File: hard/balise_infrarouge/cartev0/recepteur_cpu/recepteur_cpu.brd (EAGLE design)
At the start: 55.6 x 47 mm, 14 parts, among them U1 ARDUINO_SHIELDNO_SILK

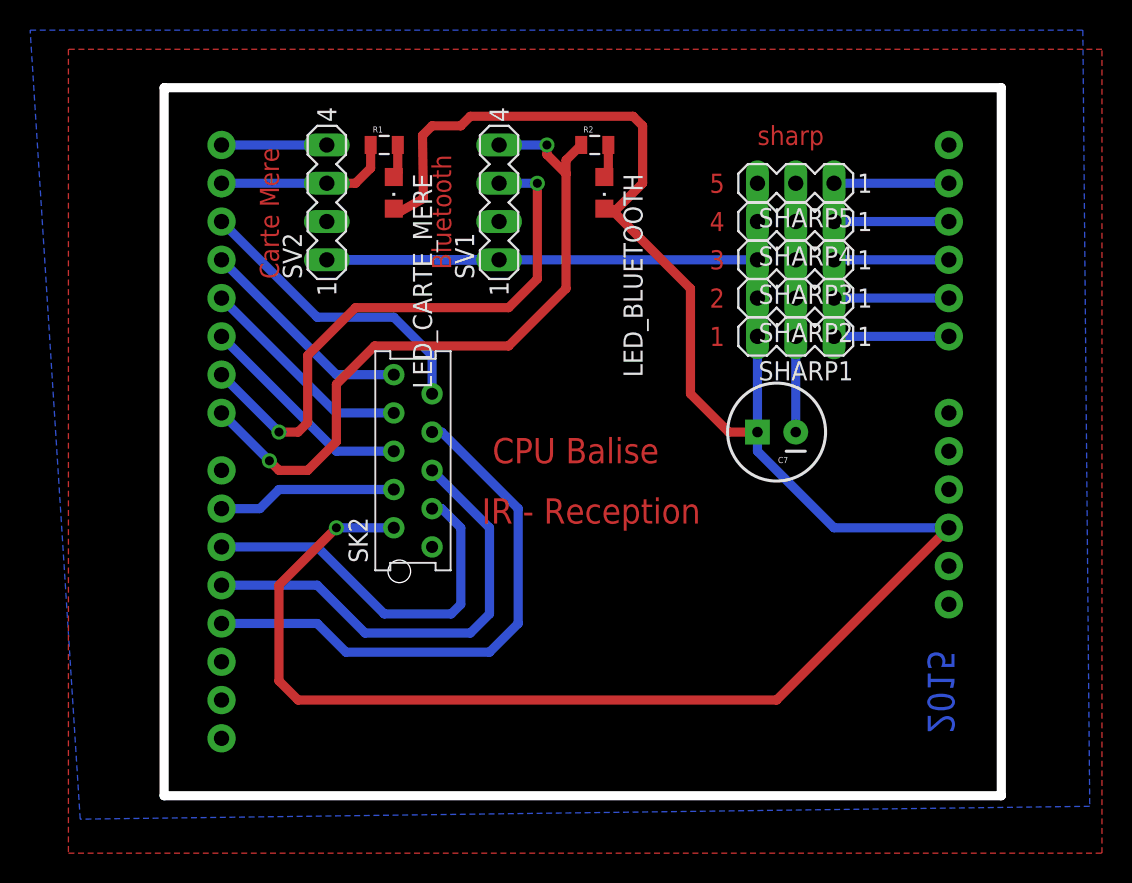
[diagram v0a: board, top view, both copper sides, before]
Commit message: maj carte extension nucleo
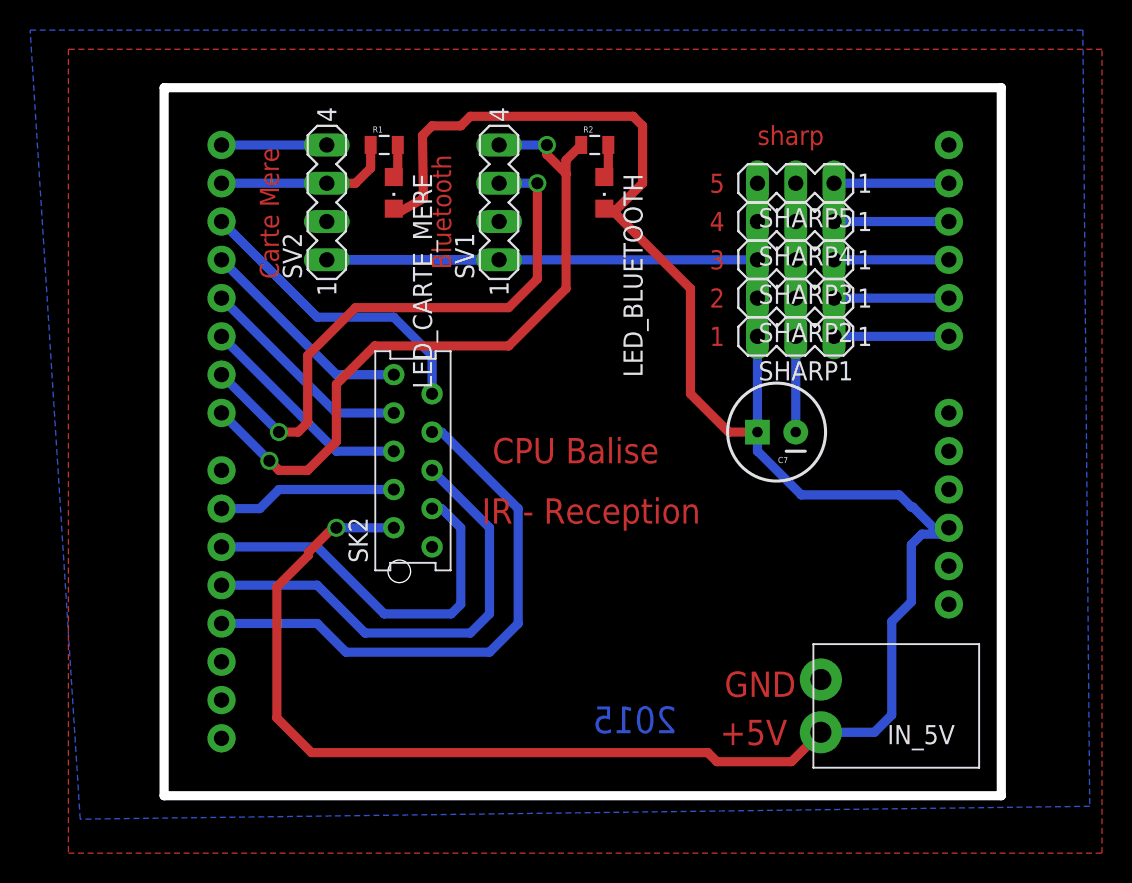
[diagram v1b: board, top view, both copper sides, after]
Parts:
- added IN_5V: SL-3.5-2-90G, WEIDMULLER:SL-3.5-2-90G
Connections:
- net +5V: now also IN_5V.2
- net GND: now also IN_5V.1
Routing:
- net +5V: track 186.7 -> 198.0 mm
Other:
- board text added: "+5V"
- board text added: "GND"
